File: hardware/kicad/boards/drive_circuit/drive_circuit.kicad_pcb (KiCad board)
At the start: 2 copper layers, 134 x 60 mm, 14 parts, among them J1 PWM ind, J2 forsyning, M1 Motor_DC, Q1 IRF540N, U1 ILD74, U2 IR2110

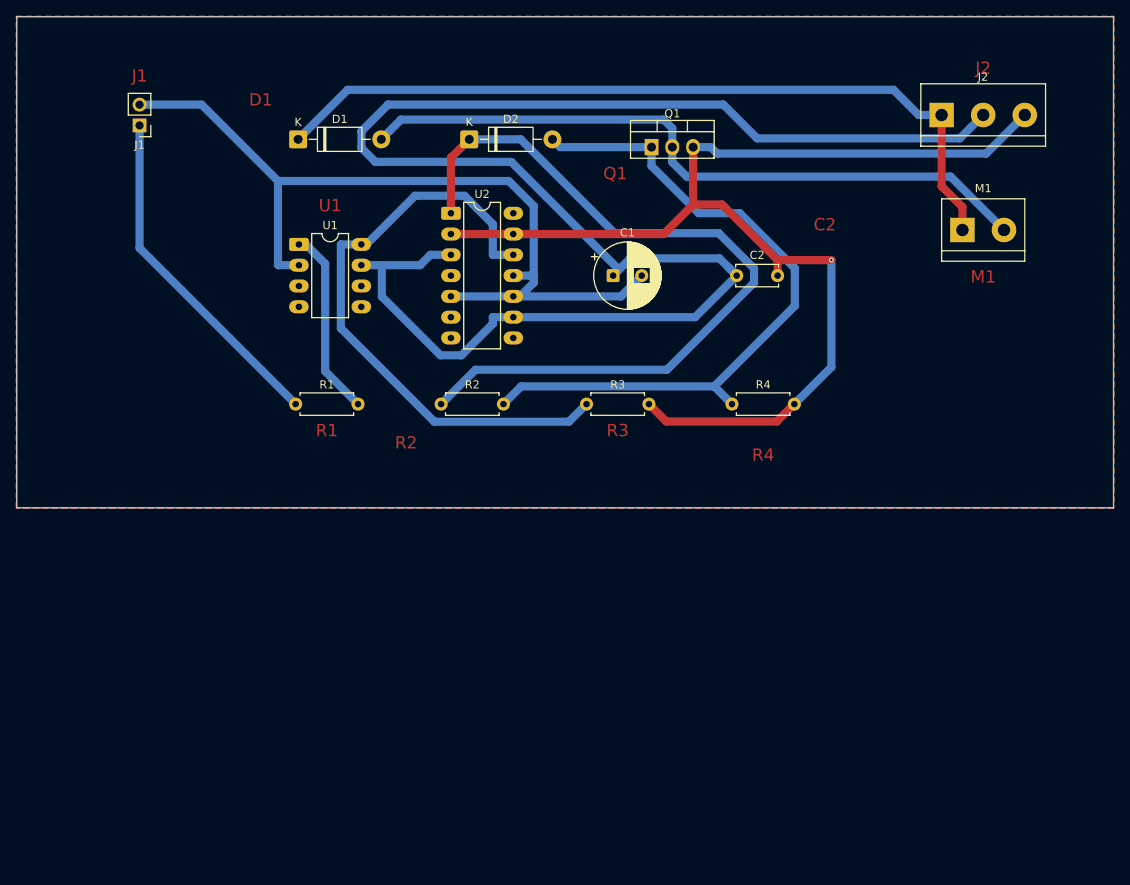
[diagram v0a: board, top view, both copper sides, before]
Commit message: Move all boards to the 104x104 jig format with compact placement
The laser positioning jig takes an exactly 109x109 mm copper blank, so every
board now has identical 104x104 edge cuts (2.5 mm rim). pcb_build.py:
- fixed JIG_W/JIG_H outline, hard failure if content overflows the square
- compact packing: 5 mm bbox gaps (was 8), squarish component cluster below
  the connector zone instead of full-width rows
- mppt/current_sense PLACE layouts re-arranged for the square and tightened

All 7 boards rerouted: 0 unconnected, 0 real DRC errors, and no vias needed
anywhere (the square format routes better than the old elongated boards).
Production DXF/gerbers re-exported; README run-plan updated for the jig
(cut blanks to exactly 109x109, all boards share the same size now).
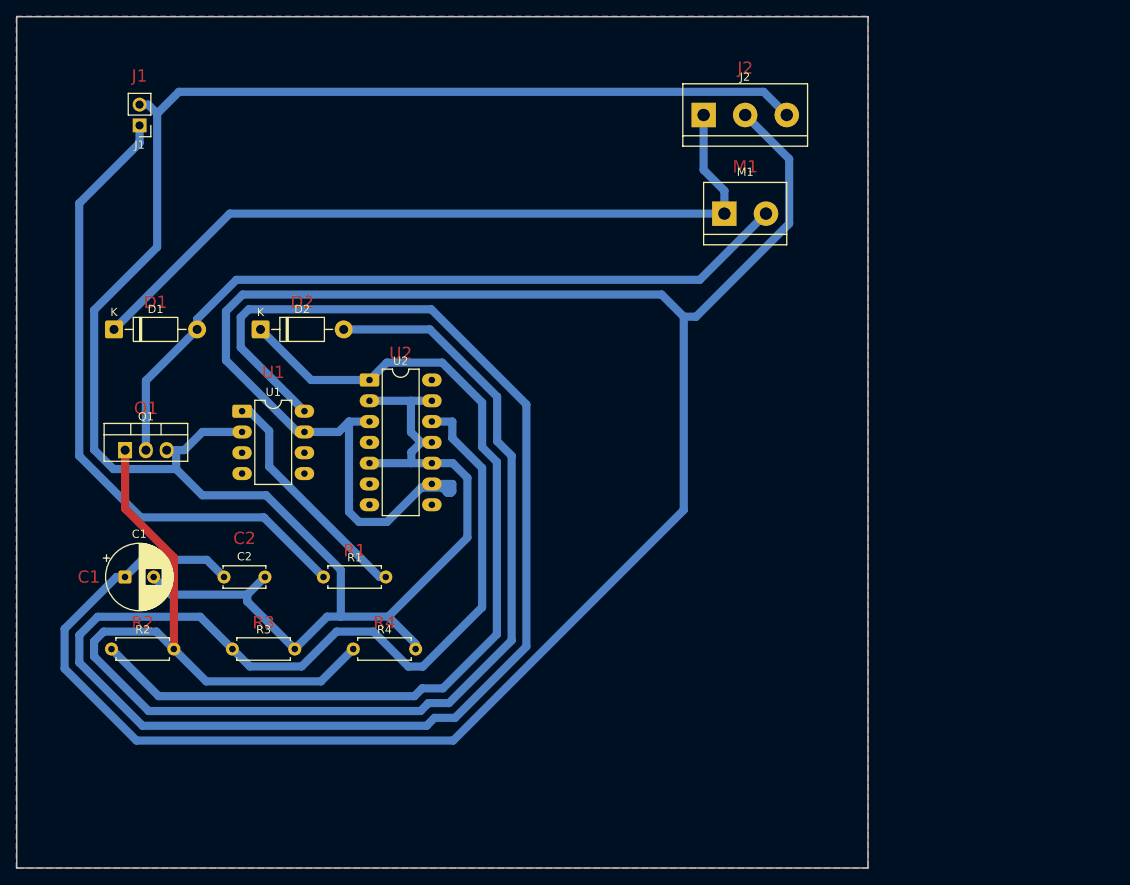
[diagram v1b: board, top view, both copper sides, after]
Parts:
- moved Q1 74.2 mm to (33.2, 73.0)
- moved C2 72.7 mm to (45.3, 88.5)
- moved C1 70.1 mm to (33.2, 88.5)
- moved R4 55.1 mm to (61.1, 97.2)
- moved R3 52.6 mm to (46.3, 97.2)
- moved R2 50.2 mm to (31.6, 97.2)
- moved D2 34.5 mm to (49.8, 58.2)
- moved D1 32.3 mm to (31.9, 58.2)
- moved M1 29.1 mm to (106.5, 44.0)
- moved J2 29.1 mm to (103.9, 32.0)
- moved U2 22.7 mm to (63.1, 64.4)
- moved U1 21.5 mm to (47.5, 68.2)
- moved R1 21.4 mm to (57.5, 88.5)
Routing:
- net Net-(U2-LIN): track 74.6 -> 235.5 mm
- net Net-(D2-A): track 85.7 -> 175.0 mm
- net +15V: track 204.4 -> 291.6 mm
- net PWM: track 42.0 -> 79.4 mm
- net GND: track 248.9 -> 274.5 mm, vias 1 -> 0
- net Net-(D2-K): track 97.4 -> 114.2 mm
- net Net-(D1-A): track 85.1 -> 93.4 mm
- net Net-(R1-Pad2): track 23.0 -> 28.5 mm
- net +20V: track 97.5 -> 93.5 mm
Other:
- board size 134 x 60 mm -> 104 x 104 mm
- board text added: "C1"
- board text added: "D2"
- board text added: "U2"

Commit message: Fix refdes copper-text collisions after manual drive_circuit reroute
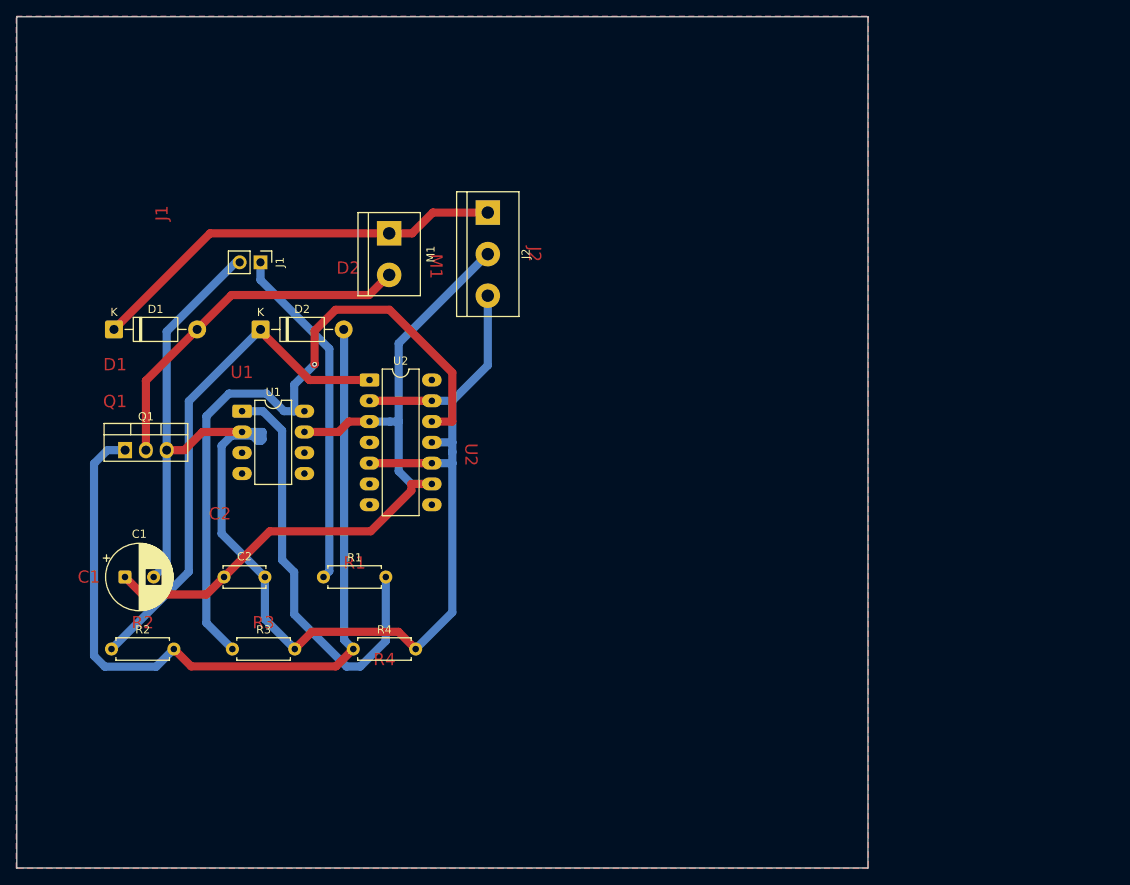
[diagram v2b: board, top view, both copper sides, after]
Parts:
- moved M1 41.0 mm to (65.5, 46.5), turned to -90 degrees
- moved J2 28.9 mm to (77.5, 43.9), turned to -90 degrees
- moved J1 22.3 mm to (49.8, 50.0), turned to -90 degrees
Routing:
- net +15V: track 291.6 -> 92.2 mm
- net Net-(U2-LIN): track 235.5 -> 84.2 mm, vias 0 -> 1
- net GND: track 274.5 -> 177.1 mm
- net Net-(D2-A): track 175.0 -> 102.4 mm
- net Net-(D2-K): track 114.2 -> 62.6 mm
- net Net-(D1-A): track 93.4 -> 43.6 mm
- net +20V: track 93.5 -> 51.6 mm
- net PWM: track 79.4 -> 42.2 mm
- net Net-(R1-Pad2): track 28.5 -> 51.9 mm

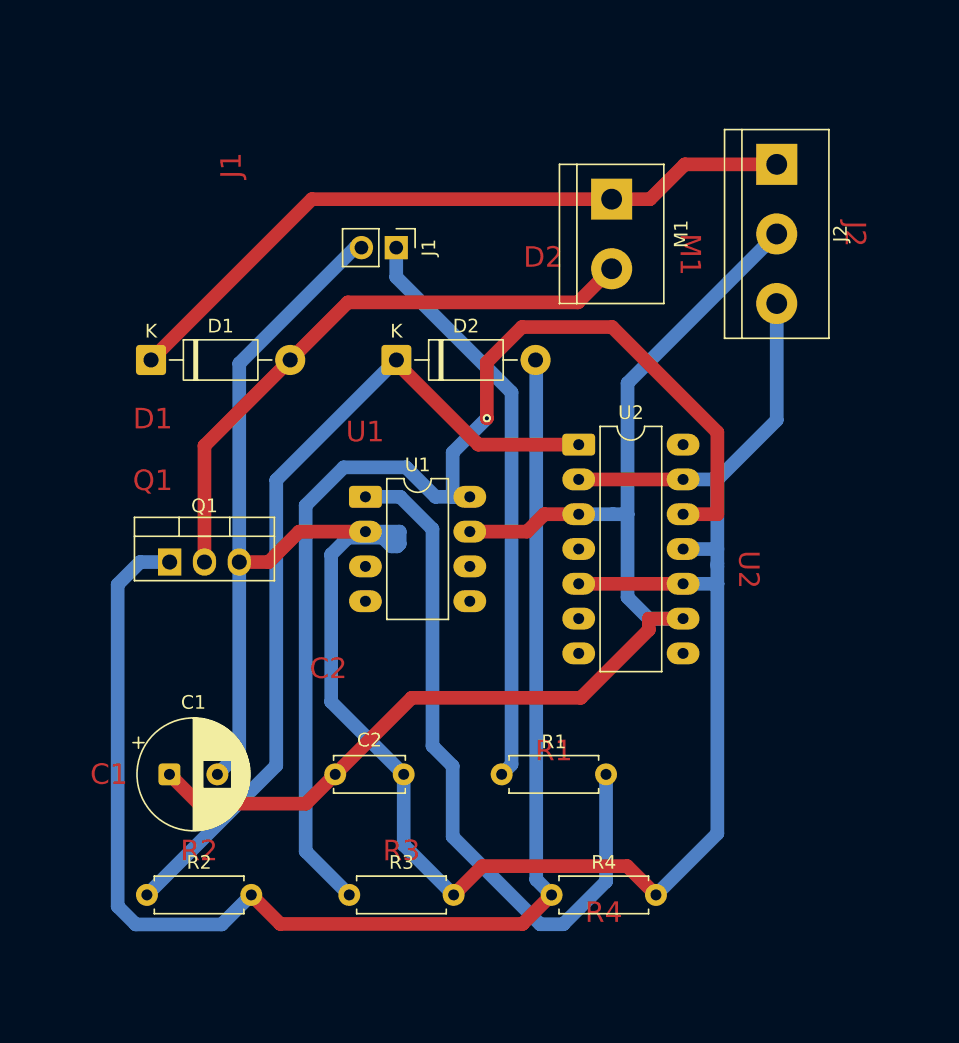
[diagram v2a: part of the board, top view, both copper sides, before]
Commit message: Condense and center all boards in the jig outline; reroute drive_circuit
Placement (pcb_build.py): connector columns now hug the component block
instead of sitting at the board edges, and the whole cluster is translated to
the center of the 104x104 outline - nothing sits next to the edge cuts
anymore. Fail-hard check if a cluster outgrows the jig.

drive_circuit keeps the hand-made GUI placement but is rerouted with the
two-stage flow: 43 top tracks + 1 via from the GUI autoroute down to 20
pin-to-pin bridges, no via. New tools/strip_routing.py removes existing
routing textually (sexpdata) - in-process pcbnew Remove() access-violates.

All 7 boards: 0 unconnected, 0 real DRC errors, no vias anywhere; buck is
now fully single-sided (0 top tracks). Production files re-exported.
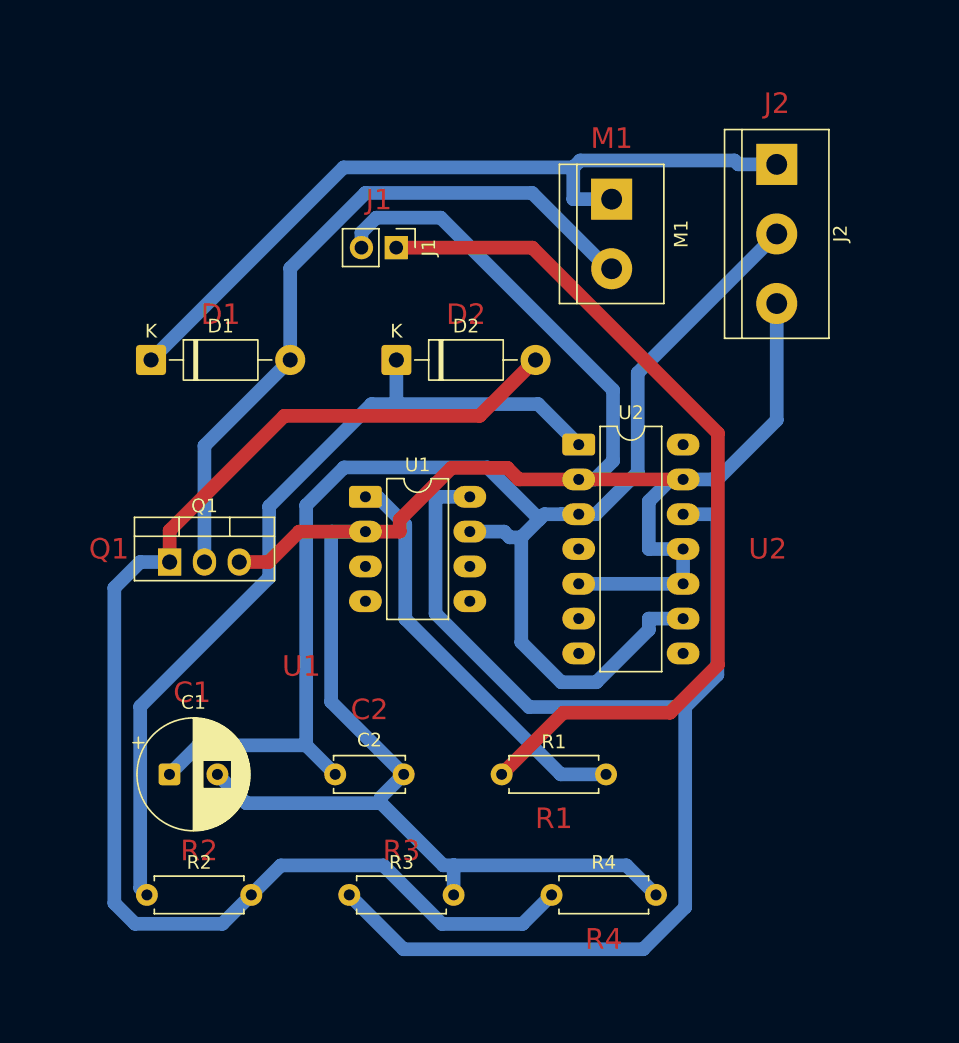
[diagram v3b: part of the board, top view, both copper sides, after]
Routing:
- net PWM: track 42.2 -> 65.1 mm
- net Net-(R1-Pad2): track 51.9 -> 30.0 mm
- net +15V: track 92.2 -> 110.2 mm
- net Net-(D1-A): track 43.6 -> 52.1 mm
- net GND: track 177.1 -> 168.9 mm
- net Net-(U2-LIN): track 84.2 -> 91.7 mm, vias 1 -> 0
- net +20V: track 51.6 -> 56.9 mm
- net Net-(D2-A): track 102.4 -> 99.0 mm

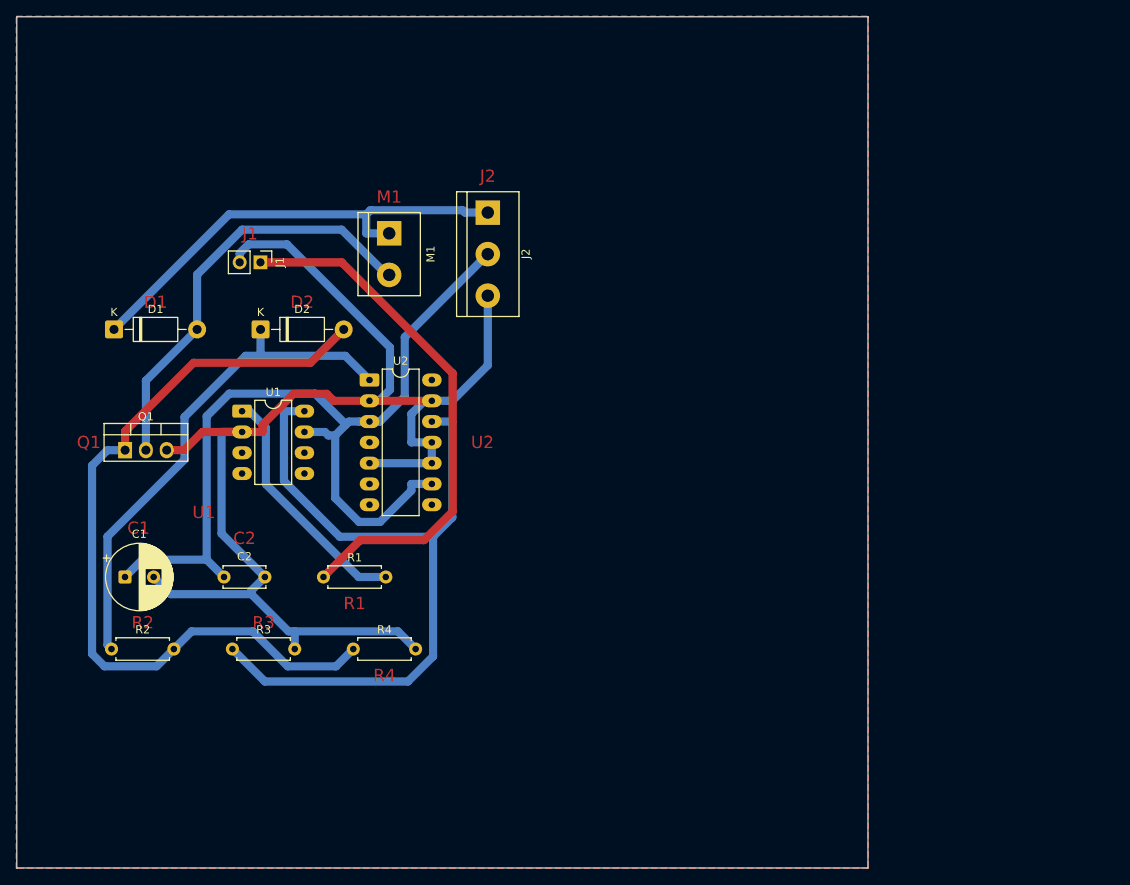
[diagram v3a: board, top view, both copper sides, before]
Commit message: drive_circuit: route board + CNC production files for the SRM-20
Routed single-sided for milling. Exported the mill production set: B.Cu +
Edge.Cuts gerbers and split PTH/NPTH drill, plus the traces/drill/cutout
toolpaths in both .nc (G-code) and .rml. Dropped the laser-only F.Cu /
mask / silk gerbers and the combined drill the mill doesn't use.
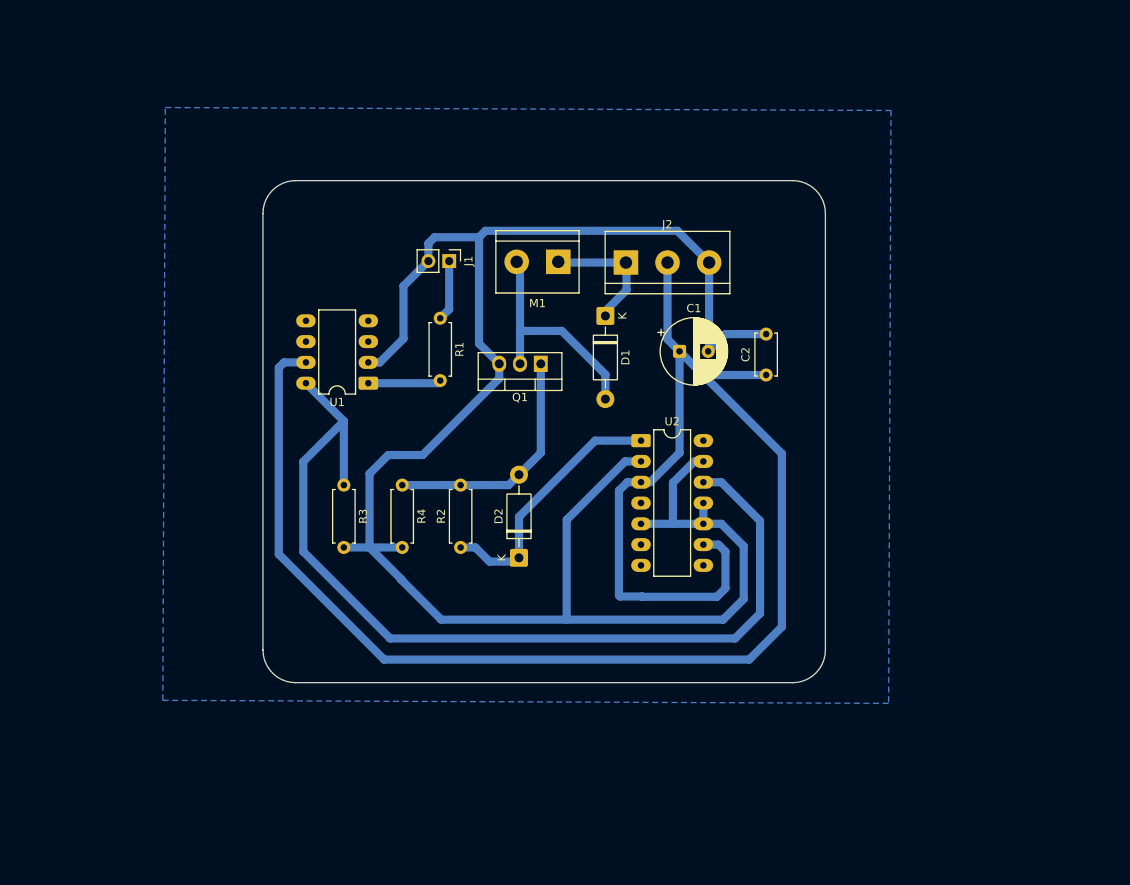
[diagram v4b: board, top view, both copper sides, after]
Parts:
- moved C1 73.2 mm to (101.0, 60.9)
- moved C2 70.7 mm to (111.6, 63.8), turned to 90 degrees
- moved D1 60.1 mm to (91.9, 56.5), turned to -90 degrees
- moved Q1 51.9 mm to (84.0, 62.4), turned to 180 degrees
- moved R2 44.4 mm to (74.2, 84.8), turned to 90 degrees
- moved D2 42.1 mm to (81.4, 86.1), turned to 90 degrees
- moved R1 34.7 mm to (71.7, 56.8), turned to -90 degrees
- moved U2 34.0 mm to (96.3, 71.8)
- moved R3 24.2 mm to (60.0, 77.2), turned to -90 degrees
- moved J1 23.1 mm to (72.8, 49.9)
- moved M1 21.0 mm to (86.2, 49.9), turned to 180 degrees
- moved R4 20.9 mm to (67.1, 77.2), turned to -90 degrees
- moved J2 18.0 mm to (94.4, 50.0), turned to 0 degrees
- moved U1 15.8 mm to (63.0, 64.8), turned to 180 degrees
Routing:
- net +15V: track 110.2 -> 208.4 mm
- net Net-(D2-A): track 99.0 -> 29.4 mm
- net GND: track 168.9 -> 236.1 mm
- net PWM: track 65.1 -> 7.43 mm
- net +20V: track 56.9 -> 15.9 mm
- net Net-(D2-K): track 62.6 -> 31.8 mm
- net Net-(D1-A): track 52.1 -> 28.3 mm
- net Net-(U2-LIN): track 91.7 -> 114.0 mm
- net Net-(R1-Pad2): track 30.0 -> 8.92 mm
- removed copper zone on F.Cu, net (none)
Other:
- board size 104 x 104 mm -> 68.7 x 61.3 mm
- board text removed: "C1"
- board text removed: "C2"
- board text removed: "D1"
- board text removed: "D2"
- board text removed: "J1"
- board text removed: "J2"
- board text removed: "M1"
- board text removed: "Q1"
- board text removed: "R1"
- board text removed: "R2"
- board text removed: "R3"
- board text removed: "R4"
- board text removed: "U1"
- board text removed: "U2"
